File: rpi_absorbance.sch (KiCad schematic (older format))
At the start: 37 parts, among them CON1 BARREL_JACK, P1 CONN_01X06, P3 RPI_HEADER, P4 stepper_conn, P5 switch_conn, Q1 NPN, U1 R-78B5.0-1.5L, U2 MEE1S1212SC, U3 DRV8825, U4 TCA9406DCUR

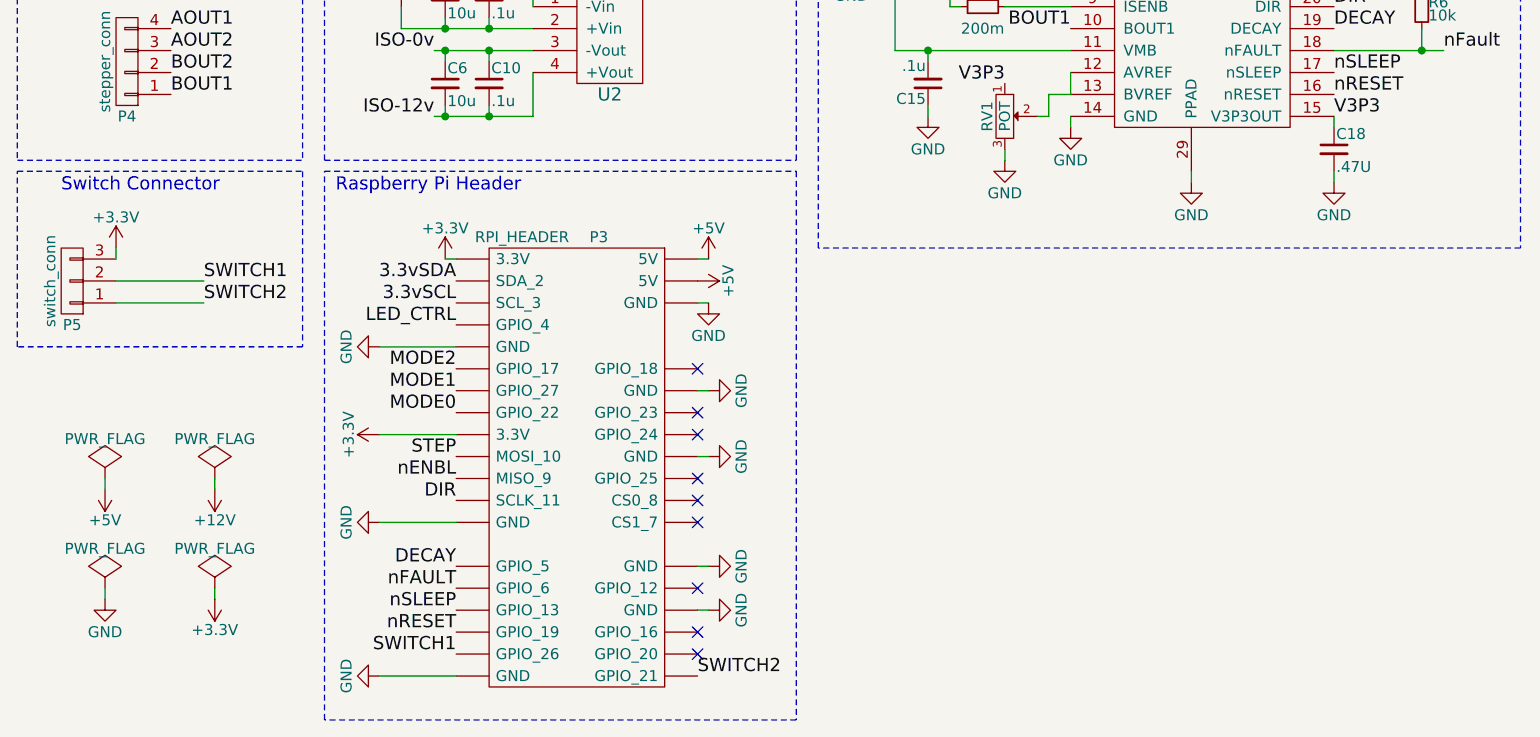
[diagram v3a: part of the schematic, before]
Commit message: Add footprints
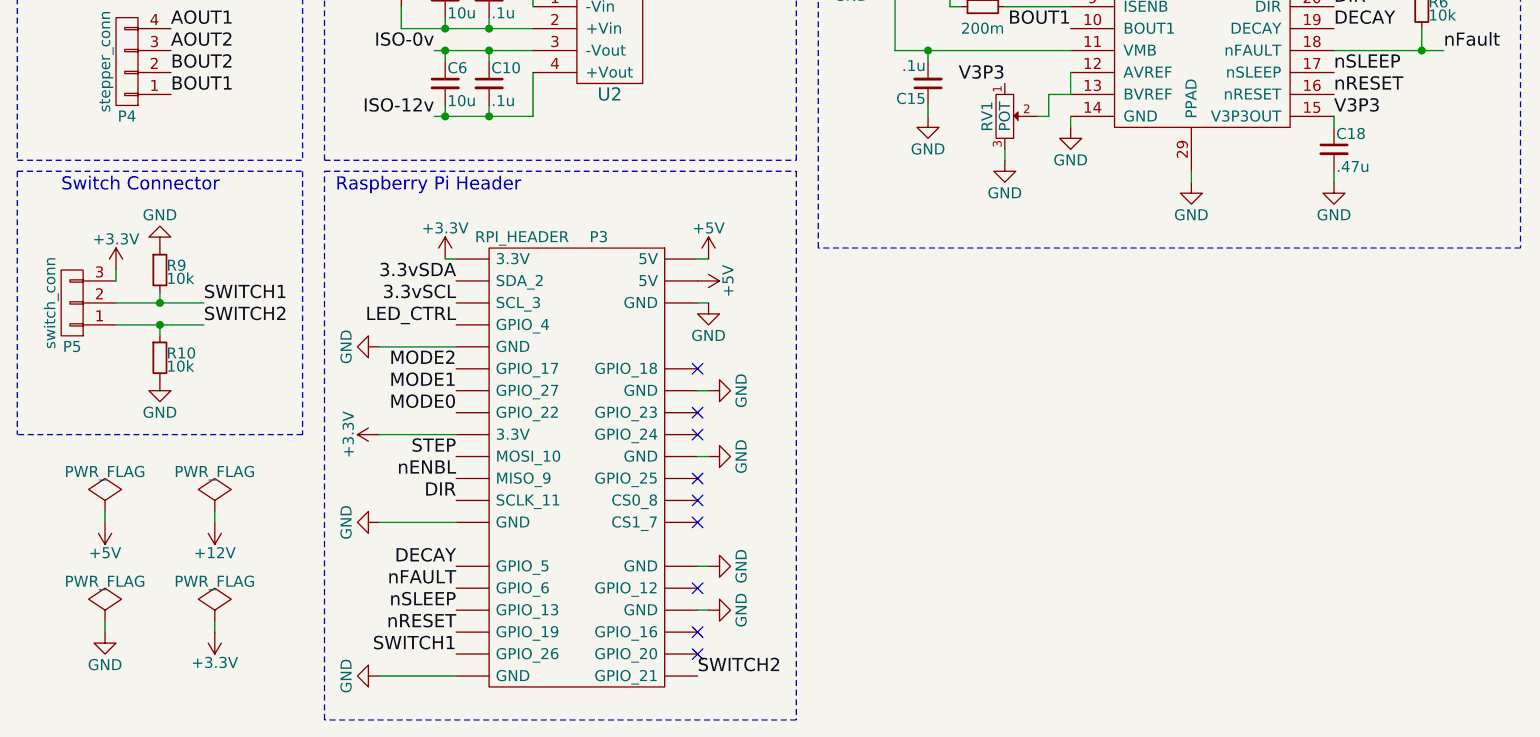
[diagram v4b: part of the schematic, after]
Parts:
- added R10, R9: 10k, Resistors_SMD:R_0603, symbol R_Small
- C18: value .47U -> .47u
- Q1: footprint TO_SOT_Packages_SMD:SOT-23 -> footprints:3-CP
- U2: footprint (none) -> footprints:MEE1-4-SIP
- U3: footprint (none) -> footprints:28-HTSSOP
- U4: footprint (none) -> footprints:8-VSSOP
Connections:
- net GND: now also R10.2, R9.1
- net SWITCH1: now also R9.2
- net SWITCH2: now also R10.1
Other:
- moved on the sheet: P5
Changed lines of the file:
@@
 F 0 "U3" H 6550 4700 60  0000 C CNN
 F 1 "DRV8825" H 6250 4700 60  0000 C CNN
-F 2 "" H 5600 3700 60  0001 C CNN
+F 2 "footprints:28-HTSSOP" H 5600 3700 60  0001 C CNN
 F 3 "" H 5600 3700 60  0000 C CNN
 	1    6450 3950
@@
 F 0 "U2" H 3800 4000 60  0000 C CNN
 F 1 "MEE1S1212SC" H 3850 4500 60  0000 C CNN
-F 2 "" H 3700 4500 60  0001 C CNN
+F 2 "footprints:MEE1-4-SIP" H 3700 4500 60  0001 C CNN
 F 3 "" H 3700 4500 60  0000 C CNN
 	1    3700 4250
@@
 F 0 "U4" H 6150 2000 60  0000 C CNN
 F 1 "TCA9406DCUR" H 6150 2500 60  0000 C CNN
-F 2 "" H 6200 2600 60  0001 C CNN
+F 2 "footprints:8-VSSOP" H 6200 2600 60  0001 C CNN
 F 3 "" H 6200 2600 60  0000 C CNN
 	1    6150 2250
@@
 F 0 "Q1" H 3500 3850 50  0000 R CNN
 F 1 "NPN" H 3500 3550 50  0000 R CNN
-F 2 "TO_SOT_Packages_SMD:SOT-23" H 3750 3800 50  0001 C CNN
+F 2 "footprints:3-CP" H 3750 3800 50  0001 C CNN
 F 3 "" H 3550 3700 50  0000 C CNN
 	1    3550 3700
@@
 L PWR_FLAG #FLG029
 U 1 1 56CC8492
-P 1500 6250
-F 0 "#FLG029" H 1500 6345 50  0001 C CNN
-F 1 "PWR_FLAG" H 1500 6430 50  0000 C CNN
-F 2 "" H 1500 6250 50  0000 C CNN
-F 3 "" H 1500 6250 50  0000 C CNN
-	1    1500 6250
+P 1500 6400
+F 0 "#FLG029" H 1500 6495 50  0001 C CNN
+F 1 "PWR_FLAG" H 1500 6580 50  0000 C CNN
+F 2 "" H 1500 6400 50  0000 C CNN
+F 3 "" H 1500 6400 50  0000 C CNN
+	1    1500 6400
 	1    0    0    -1
 $EndComp
@@
 L +5V #PWR030
 U 1 1 56CC84E3
-P 1500 6300
-F 0 "#PWR030" H 1500 6150 50  0001 C CNN
-F 1 "+5V" H 1500 6440 50  0000 C CNN
-F 2 "" H 1500 6300 50  0000 C CNN
-F 3 "" H 1500 6300 50  0000 C CNN
-	1    1500 6300
+P 1500 6450
+F 0 "#PWR030" H 1500 6300 50  0001 C CNN
+F 1 "+5V" H 1500 6590 50  0000 C CNN
+F 2 "" H 1500 6450 50  0000 C CNN
+F 3 "" H 1500 6450 50  0000 C CNN
+	1    1500 6450
 	-1   0    0    1
 $EndComp
@@
 L +12V #PWR031
 U 1 1 56CC852D
-P 2000 6300
-F 0 "#PWR031" H 2000 6150 50  0001 C CNN
-F 1 "+12V" H 2000 6440 50  0000 C CNN
-F 2 "" H 2000 6300 50  0000 C CNN
-F 3 "" H 2000 6300 50  0000 C CNN
-	1    2000 6300
+P 2000 6450
+F 0 "#PWR031" H 2000 6300 50  0001 C CNN
+F 1 "+12V" H 2000 6590 50  0000 C CNN
+F 2 "" H 2000 6450 50  0000 C CNN
+F 3 "" H 2000 6450 50  0000 C CNN
+	1    2000 6450
 	-1   0    0    1
 $EndComp
@@
 L GND #PWR032
 U 1 1 56CC8577
-P 1500 6800
-F 0 "#PWR032" H 1500 6550 50  0001 C CNN
-F 1 "GND" H 1500 6650 50  0000 C CNN
-F 2 "" H 1500 6800 50  0000 C CNN
-F 3 "" H 1500 6800 50  0000 C CNN
-	1    1500 6800
+P 1500 6950
+F 0 "#PWR032" H 1500 6700 50  0001 C CNN
+F 1 "GND" H 1500 6800 50  0000 C CNN
+F 2 "" H 1500 6950 50  0000 C CNN
+F 3 "" H 1500 6950 50  0000 C CNN
+	1    1500 6950
 	1    0    0    -1
 $EndComp
@@
 L +3.3V #PWR033
 U 1 1 56CC85C1
-P 2000 6800
-F 0 "#PWR033" H 2000 6650 50  0001 C CNN
-F 1 "+3.3V" H 2000 6940 50  0000 C CNN
-F 2 "" H 2000 6800 50  0000 C CNN
-F 3 "" H 2000 6800 50  0000 C CNN
-	1    2000 6800
+P 2000 6950
+F 0 "#PWR033" H 2000 6800 50  0001 C CNN
+F 1 "+3.3V" H 2000 7090 50  0000 C CNN
+F 2 "" H 2000 6950 50  0000 C CNN
+F 3 "" H 2000 6950 50  0000 C CNN
+	1    2000 6950
 	-1   0    0    1
 $EndComp
@@
 L PWR_FLAG #FLG034
 U 1 1 56CC860B
-P 2000 6250
-F 0 "#FLG034" H 2000 6345 50  0001 C CNN
-F 1 "PWR_FLAG" H 2000 6430 50  0000 C CNN
-F 2 "" H 2000 6250 50  0000 C CNN
-F 3 "" H 2000 6250 50  0000 C CNN
-	1    2000 6250
+P 2000 6400
+F 0 "#FLG034" H 2000 6495 50  0001 C CNN
+F 1 "PWR_FLAG" H 2000 6580 50  0000 C CNN
+F 2 "" H 2000 6400 50  0000 C CNN
+F 3 "" H 2000 6400 50  0000 C CNN
+	1    2000 6400
 	1    0    0    -1
 $EndComp
@@
 L PWR_FLAG #FLG035
 U 1 1 56CC8655
-P 1500 6750
-F 0 "#FLG035" H 1500 6845 50  0001 C CNN
-F 1 "PWR_FLAG" H 1500 6930 50  0000 C CNN
-F 2 "" H 1500 6750 50  0000 C CNN
-F 3 "" H 1500 6750 50  0000 C CNN
-	1    1500 6750
+P 1500 6900
+F 0 "#FLG035" H 1500 6995 50  0001 C CNN
+F 1 "PWR_FLAG" H 1500 7080 50  0000 C CNN
+F 2 "" H 1500 6900 50  0000 C CNN
+F 3 "" H 1500 6900 50  0000 C CNN
+	1    1500 6900
 	1    0    0    -1
 $EndComp
@@
 L PWR_FLAG #FLG036
 U 1 1 56CC88FF
-P 2000 6750
-F 0 "#FLG036" H 2000 6845 50  0001 C CNN
-F 1 "PWR_FLAG" H 2000 6930 50  0000 C CNN
-F 2 "" H 2000 6750 50  0000 C CNN
-F 3 "" H 2000 6750 50  0000 C CNN
-	1    2000 6750
+P 2000 6900
+F 0 "#FLG036" H 2000 6995 50  0001 C CNN
+F 1 "PWR_FLAG" H 2000 7080 50  0000 C CNN
+F 2 "" H 2000 6900 50  0000 C CNN
+F 3 "" H 2000 6900 50  0000 C CNN
+	1    2000 6900
 	1    0    0    -1
 $EndComp
@@
 L CONN_01X03 P5
 U 1 1 56CCA92E
-P 1350 5350
-F 0 "P5" H 1350 5550 50  0000 C CNN
-F 1 "switch_conn" V 1450 5350 50  0000 C CNN
-F 2 "Pin_Headers:Pin_Header_Straight_1x03" H 1350 5350 50  0001 C CNN
-F 3 "" H 1350 5350 50  0000 C CNN
-	1    1350 5350
+P 1350 5450
+F 0 "P5" H 1350 5650 50  0000 C CNN
+F 1 "switch_conn" V 1450 5450 50  0000 C CNN
+F 2 "Pin_Headers:Pin_Header_Straight_1x03" H 1350 5450 50  0001 C CNN
+F 3 "" H 1350 5450 50  0000 C CNN
+	1    1350 5450
 	-1   0    0    1
 $EndComp
@@
 	2750 5650 3100 5650
 Wire Wire Line
-	2000 6250 2000 6300
-Wire Wire Line
-	1500 6250 1500 6300
-Wire Wire Line
-	1500 6750 1500 6800
-Wire Wire Line
-	2000 6750 2000 6800
+	2000 6400 2000 6450
+Wire Wire Line
+	1500 6400 1500 6450
+Wire Wire Line
+	1500 6900 1500 6950
+Wire Wire Line
+	2000 6900 2000 6950
 Wire Notes Line
 	1100 4800 2400 4800
@@
 Wire Notes Line
 	1100 4850 2400 4850
-Wire Notes Line
-	2400 4850 2400 5650
-Wire Notes Line
-	2400 5650 1100 5650
 Wire Wire Line
 	5850 3250 5850 3400
@@
 P 7100 4750
 F 0 "C18" H 7110 4820 50  0000 L CNN
-F 1 ".47U" H 7110 4670 50  0000 L CNN
+F 1 ".47u" H 7110 4670 50  0000 L CNN
 F 2 "Capacitors_SMD:C_0603" H 7100 4750 50  0001 C CNN
 F 3 "" H 7100 4750 50  0000 C CNN
@@
 L +3.3V #PWR047
 U 1 1 56CD7200
-P 1550 5200
-F 0 "#PWR047" H 1550 5050 50  0001 C CNN
-F 1 "+3.3V" H 1550 5340 50  0000 C CNN
-F 2 "" H 1550 5200 50  0000 C CNN
-F 3 "" H 1550 5200 50  0000 C CNN
-	1    1550 5200
-	1    0    0    -1
-$EndComp
-Wire Wire Line
-	1550 5200 1550 5250
-Text Label 1950 5350 0    60   ~ 0
+P 1550 5300
+F 0 "#PWR047" H 1550 5150 50  0001 C CNN
+F 1 "+3.3V" H 1550 5440 50  0000 C CNN
+F 2 "" H 1550 5300 50  0000 C CNN
+F 3 "" H 1550 5300 50  0000 C CNN
+	1    1550 5300
+	1    0    0    -1
+$EndComp
+Wire Wire Line
+	1550 5300 1550 5350
+Text Label 1950 5450 0    60   ~ 0
 SWITCH1
-Text Label 1950 5450 0    60   ~ 0
+Text Label 1950 5550 0    60   ~ 0
 SWITCH2
 $Comp
@@
 	1100 3800 1100 4800
 Wire Notes Line
-	1100 5650 1100 4850
+	1100 4850 1100 6050
 Wire Wire Line
 	1800 2000 1800 1950
@@
 	5100 1850 5650 1850
 Wire Wire Line
-	1550 5350 1950 5350
-Wire Wire Line
-	1950 5450 1550 5450
+	1550 5450 1950 5450
+Wire Wire Line
+	1950 5550 1550 5550
+$Comp
+L R_Small R9
+U 1 1 56CEBB96
+P 1750 5300
+F 0 "R9" H 1780 5320 50  0000 L CNN
+F 1 "10k" H 1780 5260 50  0000 L CNN
+F 2 "Resistors_SMD:R_0603" H 1750 5300 50  0001 C CNN
+F 3 "" H 1750 5300 50  0000 C CNN
+	1    1750 5300
+	1    0    0    -1
+$EndComp
+$Comp
+L GND #PWR048
+U 1 1 56CEBCE7
+P 1750 5200
+F 0 "#PWR048" H 1750 4950 50  0001 C CNN
+F 1 "GND" H 1750 5050 50  0000 C CNN
+F 2 "" H 1750 5200 50  0000 C CNN
+F 3 "" H 1750 5200 50  0000 C CNN
+	1    1750 5200
+	-1   0    0    1
+$EndComp
+Wire Wire Line
+	1750 5400 1750 5450
+Connection ~ 1750 5450
+$Comp
+L R_Small R10
+U 1 1 56CED46B
+P 1750 5700
+F 0 "R10" H 1780 5720 50  0000 L CNN
+F 1 "10k" H 1780 5660 50  0000 L CNN
+F 2 "Resistors_SMD:R_0603" H 1750 5700 50  0001 C CNN
+F 3 "" H 1750 5700 50  0000 C CNN
+	1    1750 5700
+	1    0    0    -1
+$EndComp
+$Comp
+L GND #PWR049
+U 1 1 56CED57B
+P 1750 5800
+F 0 "#PWR049" H 1750 5550 50  0001 C CNN
+F 1 "GND" H 1750 5650 50  0000 C CNN
+F 2 "" H 1750 5800 50  0000 C CNN
+F 3 "" H 1750 5800 50  0000 C CNN
+	1    1750 5800
+	1    0    0    -1
+$EndComp
+Wire Wire Line
+	1750 5600 1750 5550
+Connection ~ 1750 5550
+Wire Notes Line
+	2400 4850 2400 6050
+Wire Notes Line
+	2400 6050 1100 6050
 $EndSCHEMATC

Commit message: Start pcb layout
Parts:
- P1: value CONN_01X06 -> DEVICE_CONN
- P4: value stepper_conn -> STEPPER_CONN
- P5: value switch_conn -> SWITCH_CONN
- RV1: footprint (none) -> footprints:BOURNS_3362P
- U1: footprint (none) -> footprints:R-78B-3-SIP
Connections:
- net +3V3: no longer R7.1
- net +5V: now also R7.1
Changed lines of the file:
@@
 F 0 "U1" H 3700 2150 60  0000 C CNN
 F 1 "R-78B5.0-1.5L" H 3800 2550 60  0000 C CNN
-F 2 "" H 3600 2600 60  0001 C CNN
+F 2 "footprints:R-78B-3-SIP" H 3600 2600 60  0001 C CNN
 F 3 "" H 3600 2600 60  0000 C CNN
 	1    3600 2350
@@
 L +3.3V #PWR012
 U 1 1 56CBCC74
-P 4950 1950
-F 0 "#PWR012" H 4950 1800 50  0001 C CNN
-F 1 "+3.3V" H 4950 2090 50  0000 C CNN
-F 2 "" H 4950 1950 50  0000 C CNN
-F 3 "" H 4950 1950 50  0000 C CNN
-	1    4950 1950
+P 4950 2050
+F 0 "#PWR012" H 4950 1900 50  0001 C CNN
+F 1 "+3.3V" H 4950 2190 50  0000 C CNN
+F 2 "" H 4950 2050 50  0000 C CNN
+F 3 "" H 4950 2050 50  0000 C CNN
+	1    4950 2050
 	1    0    0    -1
 $EndComp
@@
 L +5V #PWR013
 U 1 1 56CBD276
-P 7050 1850
-F 0 "#PWR013" H 7050 1700 50  0001 C CNN
-F 1 "+5V" H 7050 1990 50  0000 C CNN
-F 2 "" H 7050 1850 50  0000 C CNN
-F 3 "" H 7050 1850 50  0000 C CNN
-	1    7050 1850
+P 7050 1800
+F 0 "#PWR013" H 7050 1650 50  0001 C CNN
+F 1 "+5V" H 7050 1940 50  0000 C CNN
+F 2 "" H 7050 1800 50  0000 C CNN
+F 3 "" H 7050 1800 50  0000 C CNN
+	1    7050 1800
 	1    0    0    -1
 $EndComp
@@
 P 1600 4350
 F 0 "P4" H 1600 4600 50  0000 C CNN
-F 1 "stepper_conn" V 1700 4350 50  0000 C CNN
+F 1 "STEPPER_CONN" V 1700 4350 50  0000 C CNN
 F 2 "Pin_Headers:Pin_Header_Straight_1x04" H 1600 4350 50  0001 C CNN
 F 3 "" H 1600 4350 50  0000 C CNN
@@
 P 1350 5450
 F 0 "P5" H 1350 5650 50  0000 C CNN
-F 1 "switch_conn" V 1450 5450 50  0000 C CNN
+F 1 "SWITCH_CONN" V 1450 5450 50  0000 C CNN
 F 2 "Pin_Headers:Pin_Header_Straight_1x03" H 1350 5450 50  0001 C CNN
 F 3 "" H 1350 5450 50  0000 C CNN
@@
 	5250 2100 5250 2200
 Wire Wire Line
-	4950 1950 4950 2300
+	4950 2050 4950 2300
 Wire Wire Line
 	4950 2300 5650 2300
@@
 Connection ~ 5250 2150
 Wire Wire Line
-	7050 1850 7050 2200
+	7050 1800 7050 2200
 Wire Wire Line
 	7050 2200 6650 2200
@@
 F 0 "RV1" H 5600 4520 50  0000 C CNN
 F 1 "POT" H 5600 4600 50  0000 C CNN
-F 2 "" H 5600 4600 50  0001 C CNN
+F 2 "footprints:BOURNS_3362P" H 5600 4600 50  0001 C CNN
 F 3 "" H 5600 4600 50  0000 C CNN
 	1    5600 4600
@@
 P 1650 3150
 F 0 "P1" H 1650 3500 50  0000 C CNN
-F 1 "CONN_01X06" V 1750 3150 50  0000 C CNN
+F 1 "DEVICE_CONN" V 1750 3150 50  0000 C CNN
 F 2 "Pin_Headers:Pin_Header_Straight_1x06" H 1650 3150 50  0001 C CNN
 F 3 "" H 1650 3150 50  0000 C CNN
@@
 	5650 2050 5650 2100
 Wire Wire Line
-	6650 1850 7050 1850
-Wire Wire Line
-	4950 1950 5100 1950
-Wire Wire Line
-	5100 1950 5100 1850
-Wire Wire Line
-	5100 1850 5650 1850
-Wire Wire Line
 	1550 5450 1950 5450
 Wire Wire Line
-	1950 5550 1550 5550
+	1550 5550 1950 5550
 $Comp
 L R_Small R9
@@
 Wire Notes Line
 	2400 6050 1100 6050
+Wire Wire Line
+	7050 1800 5650 1800
+Wire Wire Line
+	5650 1800 5650 1850
+Wire Wire Line
+	6650 1850 6650 1800
+Connection ~ 6650 1800
 $EndSCHEMATC

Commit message: Revise circuit
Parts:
- removed C1, C10, C7, C8, C9: .1u, Capacitors_SMD:C_0603, symbol C_Small
- removed C4, C5, C6: 10u, Capacitors_SMD:C_0603, symbol C_Small
- removed P1: DEVICE_CONN, Pin_Headers:Pin_Header_Straight_1x06, symbol CONN_01X06
- removed P5: SWITCH_CONN, Pin_Headers:Pin_Header_Straight_1x03, symbol CONN_01X03
- removed Q1: NPN, footprints:3-CP, symbol Q_NPN_BEC
- removed R1: 500, Resistors_SMD:R_0603, symbol R_Small
- removed U2: MEE1S1212SC, footprints:MEE1-4-SIP, symbol MEE1S1212SC
- added C?: 100u, symbol C_Small
- added D?: D, symbol D
- added P?: CONN_01X02, symbol CONN_01X02
- added P?: CONN_02X08, symbol CONN_02X08
- added Q?: NPN, footprints:3-CP, symbol Q_NPN_BEC
- added R?: 500, symbol R_Small
- C13: footprint Capacitors_SMD:c_elec_8x6.7 -> Capacitors_SMD:C_1206
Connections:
- net +12V: now also C?.1, D?.1 (K), P?.1 (P1), P?.3 (P3)
- net +3V3: now also P?.15 (P15)
- net +5V: now also P?.4 (P4)
- net 5vSCL: now also P?.8 (P8)
- net 5vSDA: now also P?.6 (P6)
- net DECAY: now also P3.38 (GPIO_20); no longer P3.29 (GPIO_5)
- net DIR: now also P3.40 (GPIO_21); no longer P3.23 (SCLK_11)
- net GND: now also C?.2, P?.1 (P1), P?.10 (P10), P?.2 (P2), P?.9 (P9), Q?.2 (E)
- net MODE0: now also P3.33 (GPIO_13); no longer P3.15 (GPIO_22)
- net MODE1: now also P3.31 (GPIO_6); no longer P3.13 (GPIO_27)
- net MODE2: now also P3.29 (GPIO_5); no longer P3.11 (GPIO_17)
- net STEP: now also P3.35 (GPIO_19); no longer P3.19 (MOSI_10)
- net SWITCH1: now also P3.13 (GPIO_27), P?.11 (P11); no longer P3.37 (GPIO_26)
- net SWITCH2: now also P3.15 (GPIO_22), P?.13 (P13); no longer P3.40 (GPIO_21)
- net nENBL: now also P3.37 (GPIO_26); no longer P3.21 (MISO_9)
- net nFAULT: now also P3.36 (GPIO_16); no longer P3.31 (GPIO_6)
- net nRESET: now also P3.32 (GPIO_12); no longer P3.35 (GPIO_19)
- net nSLEEP: now also P3.26 (CS1_7); no longer P3.33 (GPIO_13)
- net PERI: now reaches P3.24 (CS0_8)
- net PERI: now also R?.2
- net LED_CTRL renamed LED1
- net LED1: now also P?.5 (P5)
- new net: Q?.1 (B), R?.1
- new net: D?.2 (A), P?.2 (P2), Q?.3 (C)
- new net GPIO10: P3.19 (MOSI_10), P?.12 (P12)
- new net GPIO11: P3.23 (SCLK_11), P?.16 (P16)
- new net GPIO9: P3.21 (MISO_9), P?.14 (P14)
- new net LED2: P3.11 (GPIO_17), P?.7 (P7)
- no-connect marks 10 -> 5
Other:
- note removed: "5V Converter"
- note removed: "Device Connector"
- note removed: "Isolated Power Converter (LED)"
- note removed: "Switch Connector"
- moved on the sheet: C2, C3, CON1, R10, R9, U1
